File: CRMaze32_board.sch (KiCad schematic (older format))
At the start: 83 parts, among them J101 CONN_01X02, J102 CONN_01X02, J103 GYRO_ADXRS_2, P102 GYRO_ADXRS_1, P103 SERIAL, P104 ENC_1_IN, P105 ENC_1_POWER, P106 ENC_2_IN, P107 ENC_2_POWER, P108 MOTOR1, P109 MOTOR2, Q101 BS107, Q102 BS107, Q103 BS107, Q104 BS107, Q105 BS107, SW101 EN, SW102 PUSH_IO_0, SW103 SW_SPDT, U101 ESP32-WROOM, U102 TPS76850, U103 TPS73633, U105 DRV8835_pololu

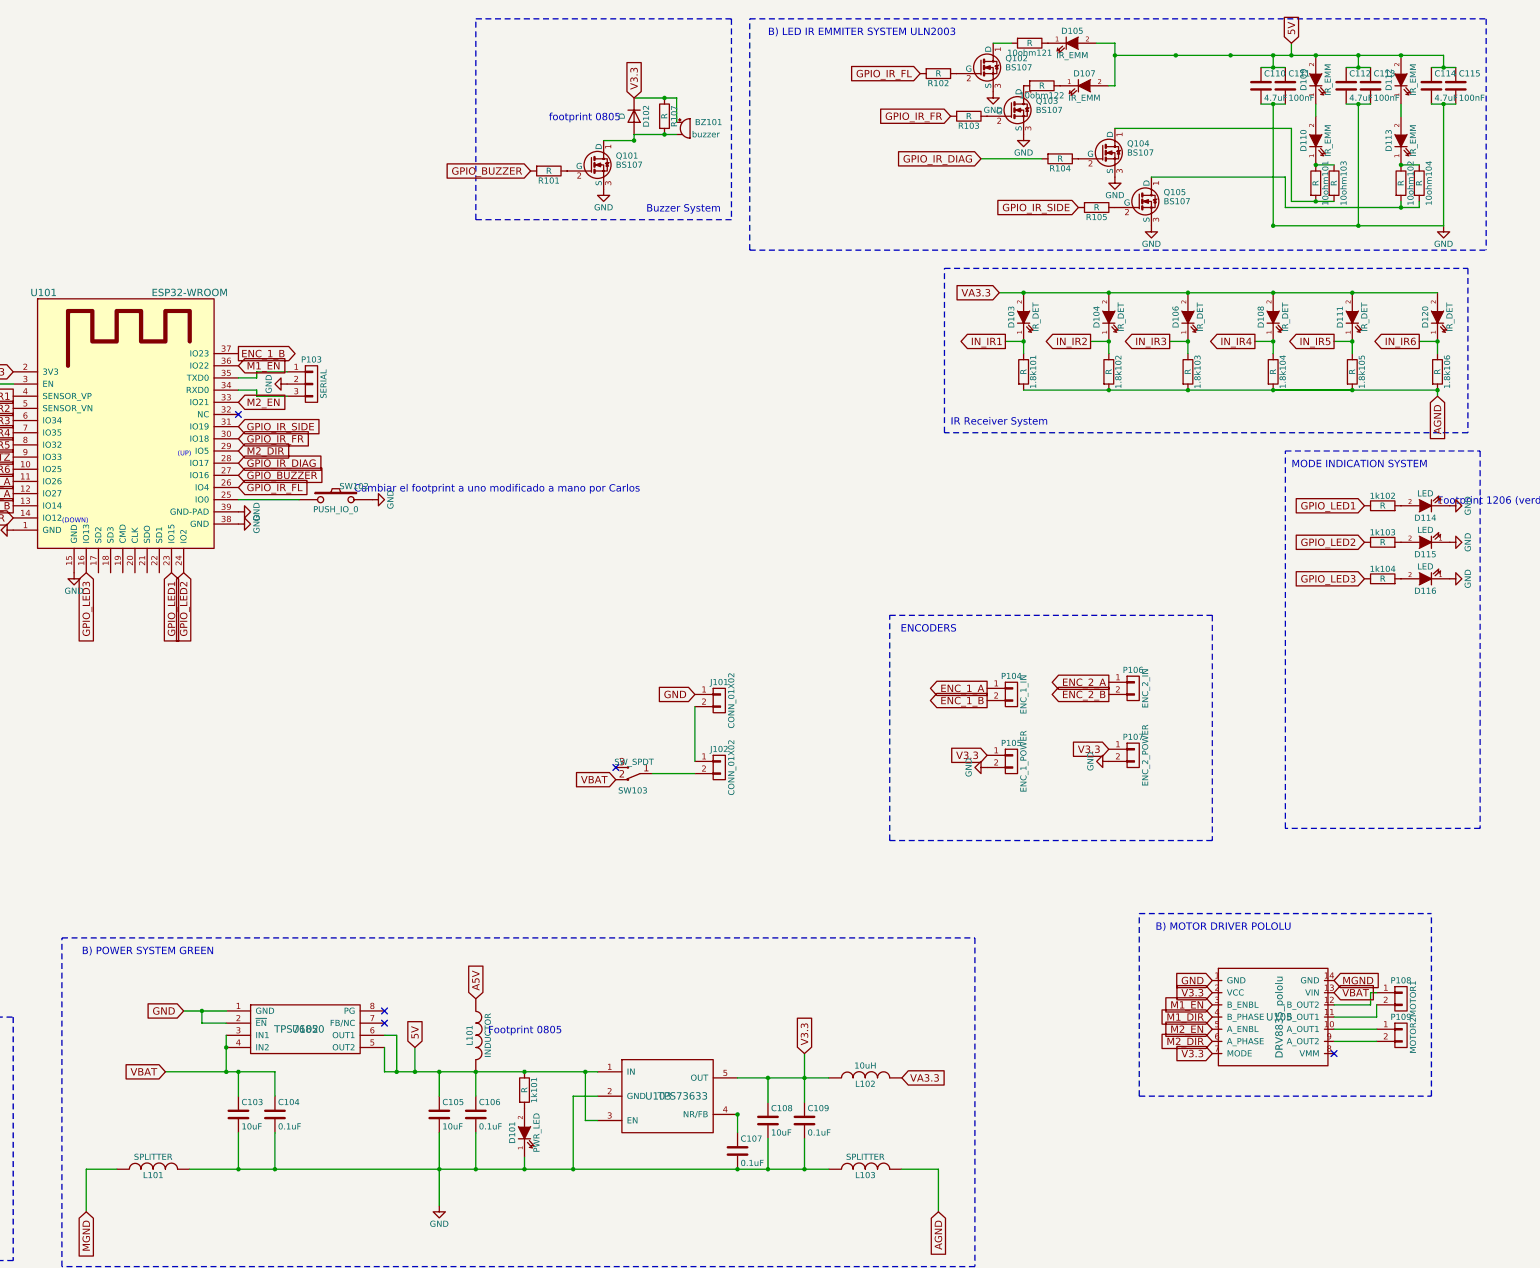
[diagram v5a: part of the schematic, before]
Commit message: arregladas referencias
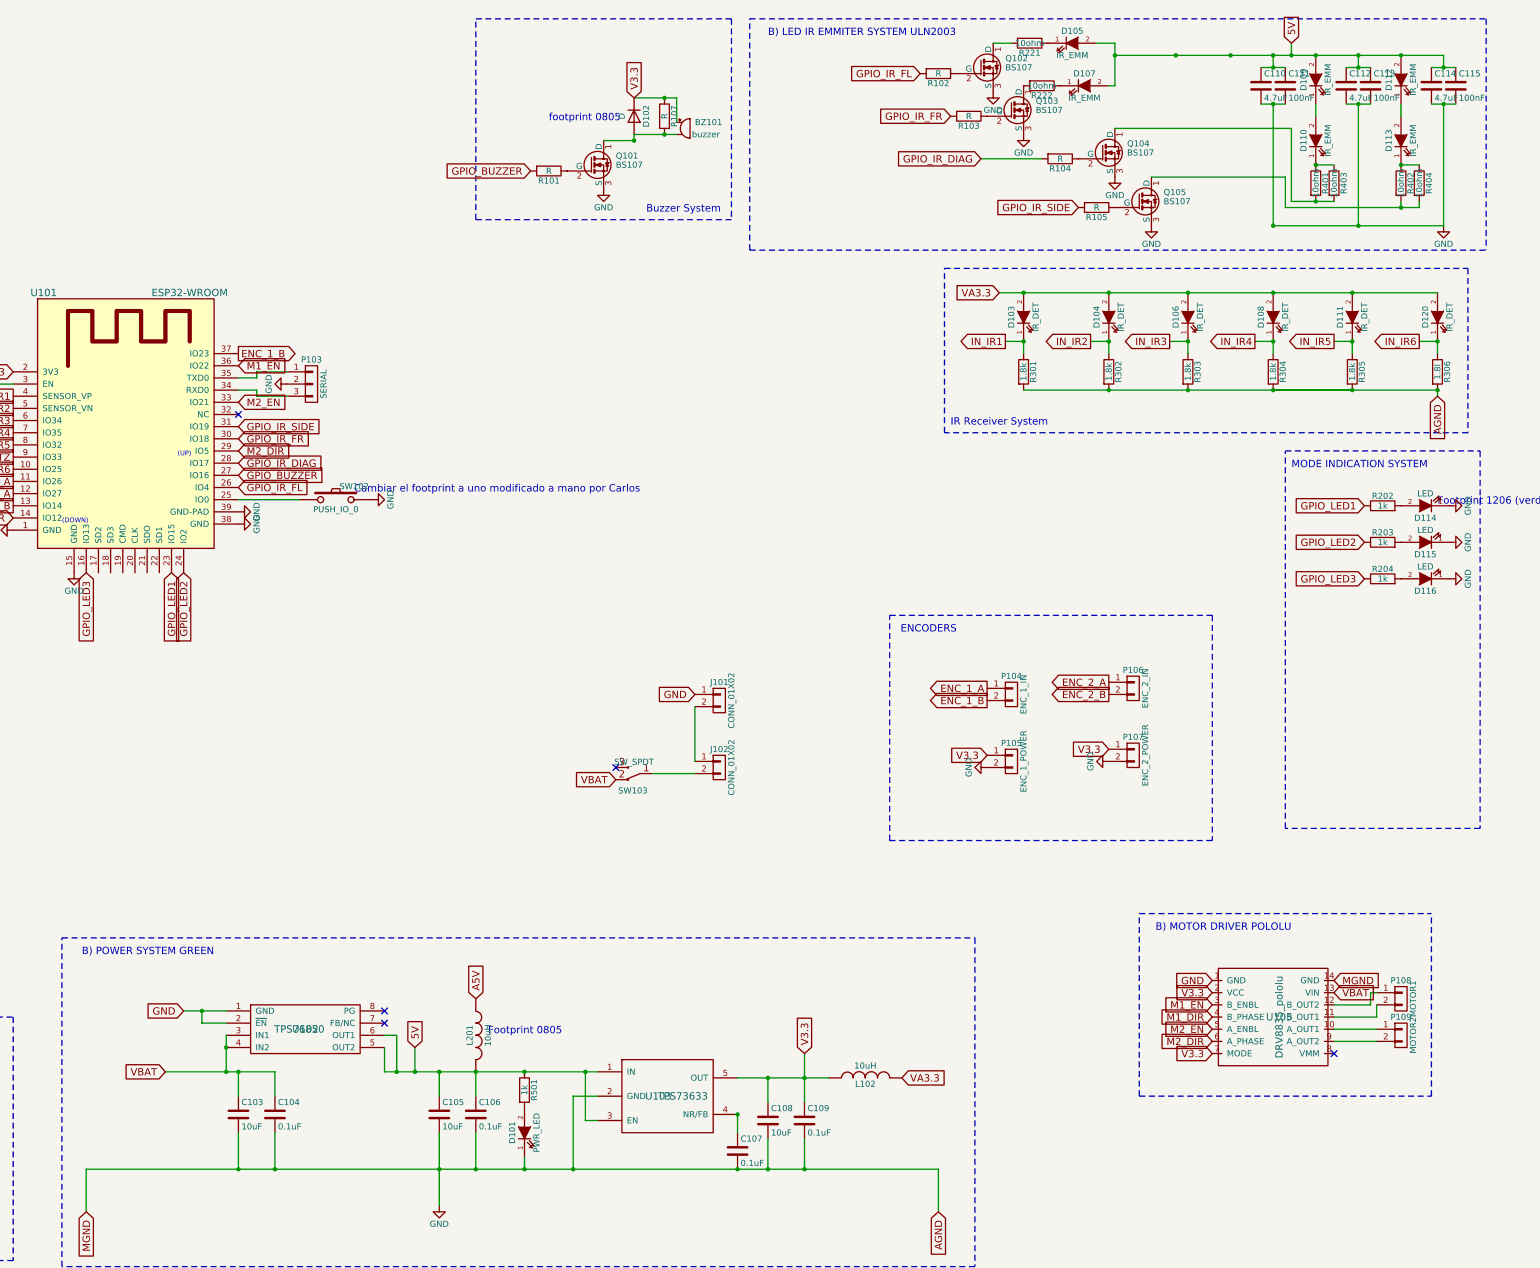
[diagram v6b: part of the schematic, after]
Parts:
- removed L101, L103: SPLITTER, Inductors_SMD:L_0805, symbol INDUCTOR-RESCUE-CRMaze32_board
- L201: renamed from L101; value INDUCTOR -> 10uH
- R202: renamed from 1k102; value R -> 1k
- R203: renamed from 1k103; value R -> 1k
- R204: renamed from 1k104; value R -> 1k
- R221: renamed from 10ohm121; value R -> 10ohm
- R222: renamed from 10ohm122; value R -> 10ohm
- R301: renamed from 1.8k101; value R -> 1.8k
- R302: renamed from 1.8k102; value R -> 1.8k
- R303: renamed from 1.8k103; value R -> 1.8k
- R304: renamed from 1.8k104; value R -> 1.8k
- R305: renamed from 1.8k105; value R -> 1.8k
- R306: renamed from 1.8k106; value R -> 1.8l
- R401: renamed from 10ohm101; value R -> 10ohm
- R402: renamed from 10ohm102; value R -> 10ohm
- R403: renamed from 10ohm103; value R -> 10ohm
- R404: renamed from 10ohm104; value R -> 10ohm
- R501: renamed from 1k101; value R -> 1k
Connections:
- net AGND is gone; now on net GND: P102.3 (P3), R301.2, R302.2, R303.2, R304.2, R305.2, R306.2
- net MGND is gone; now on net GND: U105.14 (GND)

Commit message: enrutado OK
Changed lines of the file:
@@
 OUTZ
 Text GLabel 2500 9250 1    60   Input ~ 0
-AGND
+GND
 Text GLabel 3000 9250 1    60   Input ~ 0
 A5V
@@
 V3.3
 Text GLabel 4300 10400 3    60   Input ~ 0
-MGND
-Text GLabel 11300 10400 3    60   Input ~ 0
-AGND
+GND
 $Comp
 L R R501
@@
 V3.3
 Text GLabel 14550 8500 2    60   Input ~ 0
-MGND
+GND
 Text GLabel 14550 8600 2    60   Input ~ 0
 VBAT
@@
 VA3.3
 Text GLabel 15400 3700 3    60   Input ~ 0
-AGND
+GND
 $Comp
 L GND #PWR01
@@
 Connection ~ 9050 1550
 Connection ~ 5850 10050
+Text GLabel 11300 10400 3    60   Input ~ 0
+GND
 $EndSCHEMATC
